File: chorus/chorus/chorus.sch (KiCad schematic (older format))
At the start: 17 parts, among them J1 IN, J3 Jack-DC, J4 OUT, SW1 SW_3PDT_x3, U2 TL074, U5 LM7805, U6 TL072, U8 TLE2426xLP

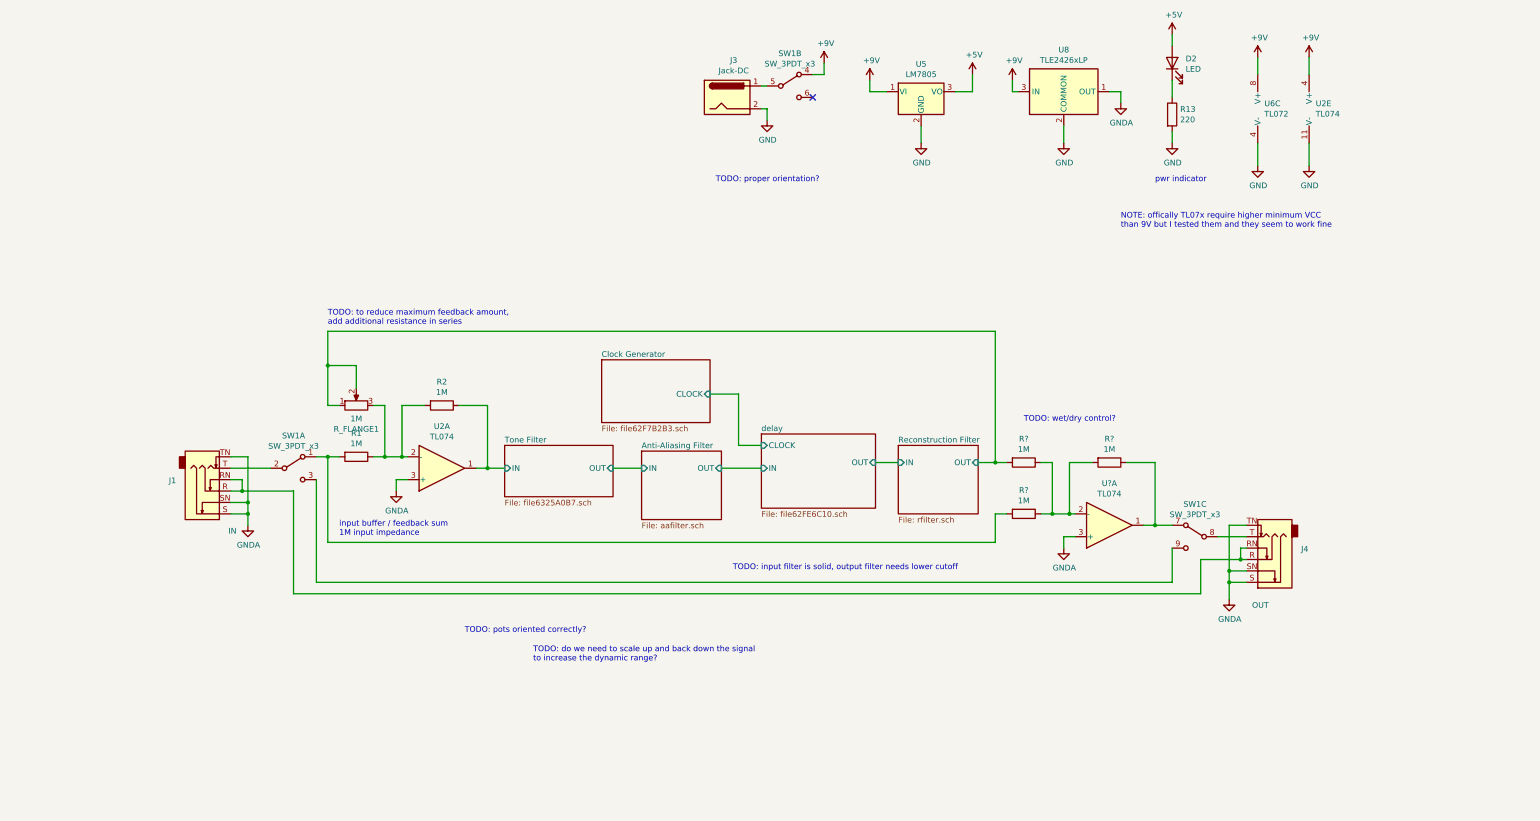
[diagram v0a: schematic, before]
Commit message: add wet/dry mix and recalculate filters
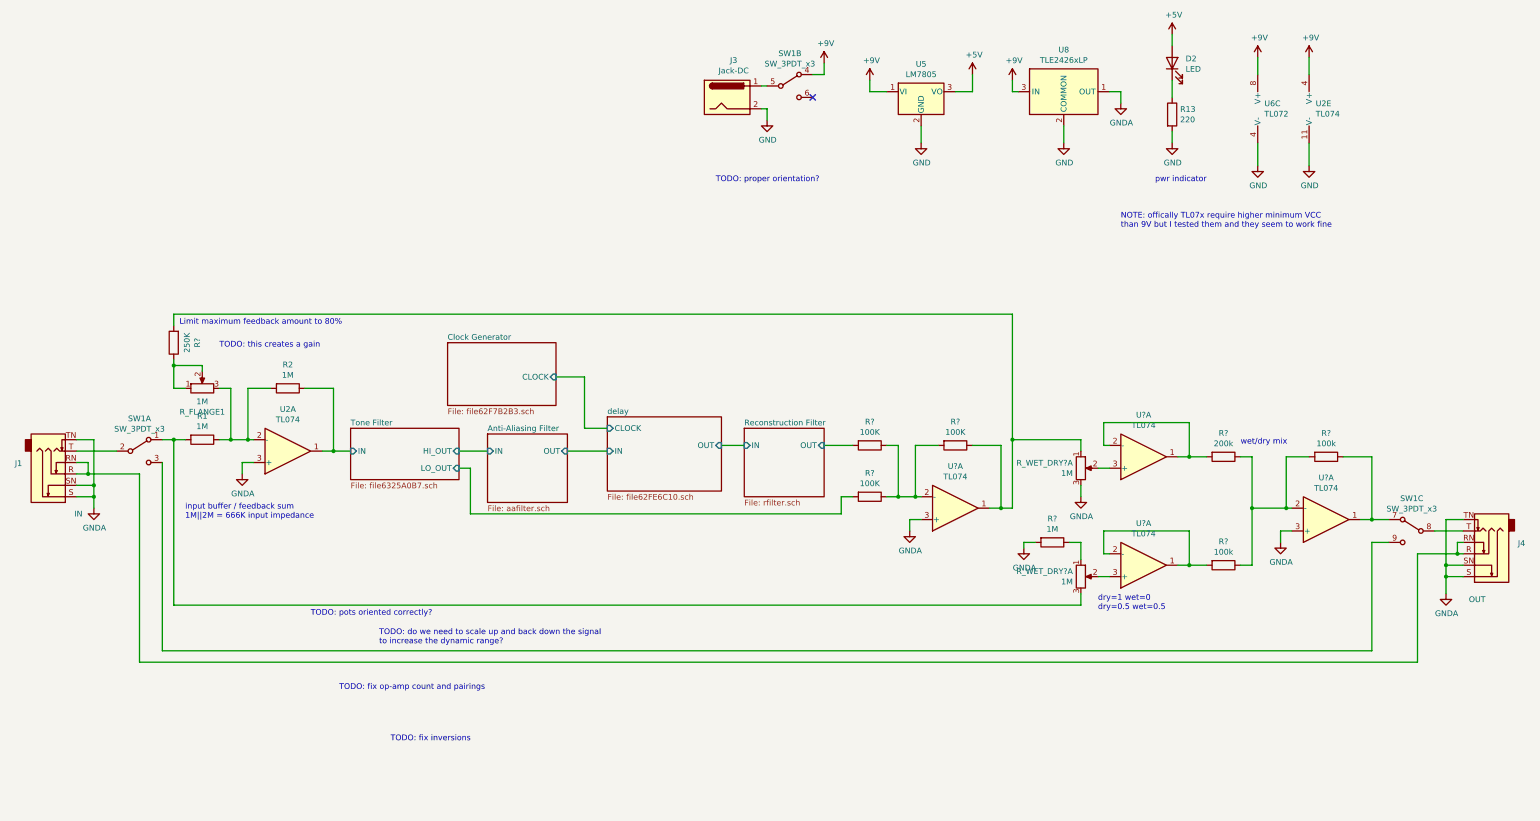
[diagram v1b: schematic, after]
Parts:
- removed R?: 1M, Resistor_THT:R_Axial_DIN0204_L3.6mm_D1.6mm_P2.54mm_Vertical, symbol Device:R
- added R?: 100K, Resistor_THT:R_Axial_DIN0204_L3.6mm_D1.6mm_P2.54mm_Vertical, symbol Device:R
- added R? (x2): 100k, Resistor_THT:R_Axial_DIN0204_L3.6mm_D1.6mm_P2.54mm_Vertical, symbol Device:R
- added R?: 1M, Resistor_THT:R_Axial_DIN0204_L3.6mm_D1.6mm_P2.54mm_Vertical, symbol Device:R
- added R?: 200k, Resistor_THT:R_Axial_DIN0204_L3.6mm_D1.6mm_P2.54mm_Vertical, symbol Device:R
- added R?: 250K, Resistor_THT:R_Axial_DIN0204_L3.6mm_D1.6mm_P2.54mm_Vertical, symbol Device:R
- added R_WET_DRY? (x2): 1M, symbol Device:R_POT_Dual_Separate
- added U? (x3): TL074, Package_DIP:DIP-14_W7.62mm, symbol Amplifier_Operational:TL074
- R? (x2): value 1M -> 100K
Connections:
- net GNDA: now also R?.2, R_WET_DRY?.3, U?.3 (+)
- net Reconstruction Filter/OUT: no longer R_FLANGE1.1, R_FLANGE1.2
- net at R1.2, SW1.1 (A): now also R_WET_DRY?.3
- net at R?.1, U?.1: now also R?.2, R_WET_DRY?.1; no longer SW1.7 (A)
- net at R?.1, R?.2, U?.2 (-): now also R?.1
- new net: R?.1, R_FLANGE1.1, R_FLANGE1.2
- new net: R?.1, SW1.7 (A), U?.1
- new net: R?.1, R?.1, R?.2, U?.2 (-)
- new net: R?.1, R_WET_DRY?.1
- new net: R?.2, U?.1, U?.2 (-) (x2)
- new net: R_WET_DRY?.2, U?.3 (+) (x2)
- new net Tone Filter/LO_OUT: R?.2
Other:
- note added: "Limit maximum feedback amount to 80%"
- note added: "TODO: fix inversions"
- note added: "TODO: fix op-amp count and pairings"
- note added: "TODO: this creates a gain"
- note added: "dry=1 wet=0\ndry=0.5 wet=0.5"
- note added: "input buffer / feedback sum\n1M||2M = 666K input impedance"
- note added: "wet/dry mix"
- note removed: "TODO: input filter is solid, output filter needs lower cutoff"
- note removed: "TODO: to reduce maximum feedback amount,\nadd additional resistance in series"
- note removed: "TODO: wet/dry control?"
- note removed: "input buffer / feedback sum\n1M input impedance"
- moved on the sheet: J1, J4, R1, R2, R?, R_FLANGE1, SW1A, SW1C, U2A, U?A

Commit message: update filters
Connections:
- net at R?.1, R_WET_DRY?.1, U?.1: no longer R?.2
- net at R?.2, U?.1, U?.2 (-): now also R?.2
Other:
- note added: "TODO: hard-code to 50/50 saves 2 op amps and a dual pot"
- note added: "TODO: probably too complex, but if tone filter became\nBP with only LP side tunable, and allowed high freqs\ncut by filters around the effect, would have a more consistent\ntone"
- note added: "filter+delay stage are all non-inverting,\nso low + high are in phase\n\ninput sum is inverting, then tone recombination is\ninverting, so wet + dry are in phase\n\nhowever end-to-end signal is inverted (by final sum/output buffer)"
- note added: "wet/dry mix\nmin: dry=1 wet=0\nmax: dry=0.5 wet=0.5"
- note removed: "TODO: fix inversions"
- note removed: "TODO: this creates a gain"
- note removed: "dry=1 wet=0\ndry=0.5 wet=0.5"
- note removed: "wet/dry mix"
- moved on the sheet: R?, U?A
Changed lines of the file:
@@
 L Amplifier_Operational:TL074 U?
 U 1 1 6282D08A
-P 7650 5050
-F 0 "U?" H 7650 4683 50  0000 C CNN
-F 1 "TL074" H 7650 4774 50  0000 C CNN
-F 2 "Package_DIP:DIP-14_W7.62mm" H 7600 5150 50  0001 C CNN
-F 3 "http://www.ti.com/lit/ds/symlink/tl071.pdf" H 7700 5250 50  0001 C CNN
-	1    7650 5050
-	1    0    0    1
-$EndComp
-Wire Wire Line
-	7250 5250 7250 5150
-Wire Wire Line
-	7250 5150 7350 5150
-Wire Wire Line
-	7350 4950 7300 4950
-Wire Wire Line
-	7300 4500 7300 4950
-Connection ~ 7300 4950
-Wire Wire Line
-	7300 4950 7150 4950
+P 7650 5200
+F 0 "U?" H 7650 4833 50  0000 C CNN
+F 1 "TL074" H 7650 4924 50  0000 C CNN
+F 2 "Package_DIP:DIP-14_W7.62mm" H 7600 5300 50  0001 C CNN
+F 3 "http://www.ti.com/lit/ds/symlink/tl071.pdf" H 7700 5400 50  0001 C CNN
+	1    7650 5200
+	1    0    0    1
+$EndComp
+Wire Wire Line
+	7250 5400 7250 5300
+Wire Wire Line
+	7250 5300 7350 5300
+Wire Wire Line
+	7350 5100 7300 5100
+Connection ~ 7300 5100
+Wire Wire Line
+	7300 5100 7150 5100
 $Comp
 L Device:R R?
 U 1 1 6282D0A4
-P 7650 4500
-F 0 "R?" V 7443 4500 50  0000 C CNN
-F 1 "100K" V 7534 4500 50  0000 C CNN
-F 2 "Resistor_THT:R_Axial_DIN0204_L3.6mm_D1.6mm_P2.54mm_Vertical" V 7580 4500 50  0001 C CNN
-F 3 "~" H 7650 4500 50  0001 C CNN
-	1    7650 4500
-	0    1    1    0
-$EndComp
-Wire Wire Line
-	7500 4500 7300 4500
-Wire Wire Line
-	7800 4500 8050 4500
-Wire Wire Line
-	8050 5050 7950 5050
+P 7650 4750
+F 0 "R?" V 7443 4750 50  0000 C CNN
+F 1 "100K" V 7534 4750 50  0000 C CNN
+F 2 "Resistor_THT:R_Axial_DIN0204_L3.6mm_D1.6mm_P2.54mm_Vertical" V 7580 4750 50  0001 C CNN
+F 3 "~" H 7650 4750 50  0001 C CNN
+	1    7650 4750
+	0    1    1    0
+$EndComp
+Wire Wire Line
+	8050 5200 7950 5200
 Wire Wire Line
 	7050 4500 7150 4500
@@
 L power:GNDA #PWR?
 U 1 1 6282D0C0
-P 7250 5250
-F 0 "#PWR?" H 7250 5000 50  0001 C CNN
-F 1 "GNDA" H 7255 5077 50  0000 C CNN
-F 2 "" H 7250 5250 50  0001 C CNN
-F 3 "" H 7250 5250 50  0001 C CNN
-	1    7250 5250
+P 7250 5400
+F 0 "#PWR?" H 7250 5150 50  0001 C CNN
+F 1 "GNDA" H 7255 5227 50  0000 C CNN
+F 2 "" H 7250 5400 50  0001 C CNN
+F 3 "" H 7250 5400 50  0001 C CNN
+	1    7250 5400
 	1    0    0    -1
 $EndComp
@@
 $EndComp
 Wire Wire Line
-	8050 5050 8050 4500
-Connection ~ 8050 5050
+	8050 5200 8050 4750
+Connection ~ 8050 5200
 Connection ~ 800  4450
 Wire Wire Line
@@
 L Device:R R?
 U 1 1 62A6A9A3
-P 6900 4950
-F 0 "R?" V 6693 4950 50  0000 C CNN
-F 1 "100K" V 6784 4950 50  0000 C CNN
-F 2 "Resistor_THT:R_Axial_DIN0204_L3.6mm_D1.6mm_P2.54mm_Vertical" V 6830 4950 50  0001 C CNN
-F 3 "~" H 6900 4950 50  0001 C CNN
-	1    6900 4950
+P 6900 5100
+F 0 "R?" V 6693 5100 50  0000 C CNN
+F 1 "100K" V 6784 5100 50  0000 C CNN
+F 2 "Resistor_THT:R_Axial_DIN0204_L3.6mm_D1.6mm_P2.54mm_Vertical" V 6830 5100 50  0001 C CNN
+F 3 "~" H 6900 5100 50  0001 C CNN
+	1    6900 5100
 	0    1    1    0
 $EndComp
@@
 Connection ~ 11300 5150
 Wire Wire Line
-	7050 4950 7150 4950
-Connection ~ 7150 4950
-Wire Wire Line
-	7150 4500 7150 4950
-Wire Wire Line
-	6750 4950 6650 4950
-Wire Wire Line
-	6650 4950 6650 5100
-Wire Wire Line
-	3400 5100 6650 5100
+	7050 5100 7150 5100
+Connection ~ 7150 5100
 Wire Wire Line
 	6500 4500 6750 4500
-Wire Wire Line
-	8150 5050 8150 4450
-Wire Wire Line
-	8150 5050 8050 5050
-Text Notes 8900 5950 0    50   ~ 0
-dry=1 wet=0\ndry=0.5 wet=0.5
-Text Notes 10150 4500 0    50   ~ 0
-wet/dry mix
+Text Notes 8800 5100 0    50   ~ 0
+wet/dry mix\nmin: dry=1 wet=0\nmax: dry=0.5 wet=0.5
 Text Notes 2250 6650 0    50   ~ 0
 TODO: fix op-amp count and pairings
-Text Notes 2700 7100 0    50   ~ 0
-TODO: fix inversions
 $Comp
 L Amplifier_Operational:TL074 U?
@@
 L power:GNDA #PWR?
 U 1 1 62B4A803
-P 8750 4950
-F 0 "#PWR?" H 8750 4700 50  0001 C CNN
-F 1 "GNDA" H 8755 4777 50  0000 C CNN
-F 2 "" H 8750 4950 50  0001 C CNN
-F 3 "" H 8750 4950 50  0001 C CNN
-	1    8750 4950
-	1    0    0    -1
+P 8750 4450
+F 0 "#PWR?" H 8750 4200 50  0001 C CNN
+F 1 "GNDA" H 8755 4277 50  0000 C CNN
+F 2 "" H 8750 4450 50  0001 C CNN
+F 3 "" H 8750 4450 50  0001 C CNN
+	1    8750 4450
+	-1   0    0    1
 $EndComp
 Wire Wire Line
@@
 Connection ~ 9700 4600
 Wire Wire Line
-	9700 4600 9850 4600
+	9700 4600 9800 4600
 $Comp
 L Device:R_POT_Dual_Separate R_WET_DRY?
@@
 F 3 "~" H 8750 4700 50  0001 C CNN
 	1    8750 4700
-	1    0    0    -1
+	1    0    0    1
 $EndComp
 Wire Wire Line
@@
 L power:GNDA #PWR?
 U 1 1 62BC944D
-P 8250 5400
-F 0 "#PWR?" H 8250 5150 50  0001 C CNN
-F 1 "GNDA" H 8255 5227 50  0000 C CNN
-F 2 "" H 8250 5400 50  0001 C CNN
-F 3 "" H 8250 5400 50  0001 C CNN
-	1    8250 5400
+P 8000 5400
+F 0 "#PWR?" H 8000 5150 50  0001 C CNN
+F 1 "GNDA" H 8005 5227 50  0000 C CNN
+F 2 "" H 8000 5400 50  0001 C CNN
+F 3 "" H 8000 5400 50  0001 C CNN
+	1    8000 5400
 	1    0    0    -1
 $EndComp
 Wire Wire Line
-	8250 5400 8250 5350
-Wire Wire Line
-	8250 5350 8350 5350
-Wire Wire Line
 	8650 5350 8750 5350
 Wire Wire Line
 	8750 5350 8750 5500
-Wire Wire Line
-	8750 4950 8750 4850
 Wire Wire Line
 	8750 5800 8750 5900
@@
 Wire Wire Line
 	10250 5050 10250 4600
-Wire Wire Line
-	8750 4550 8750 4450
-Wire Wire Line
-	8750 4450 8150 4450
-Connection ~ 8150 4450
-Wire Wire Line
-	8150 3350 8150 4450
-Wire Wire Line
-	800  3350 8150 3350
 $Comp
 L Device:R R?
@@
 Wire Wire Line
 	800  3800 800  4000
-Text Notes 1200 3650 0    50   ~ 0
-TODO: this creates a gain
 Wire Wire Line
 	700  6300 11300 6300
@@
 Wire Wire Line
 	11700 5450 11700 6400
+Wire Wire Line
+	7150 4500 7150 5100
+Wire Wire Line
+	7500 4750 7300 4750
+Wire Wire Line
+	7300 4750 7300 5100
+Wire Wire Line
+	7800 4750 8050 4750
+Wire Wire Line
+	3400 5100 6750 5100
+Wire Wire Line
+	8750 4550 8750 4450
+Wire Wire Line
+	8750 4850 8750 5200
+Wire Wire Line
+	8000 5400 8000 5350
+Wire Wire Line
+	8000 5350 8350 5350
+Text Notes 9000 6000 0    50   ~ 0
+TODO: hard-code to 50/50 saves 2 op amps and a dual pot
+Text Notes 2400 5650 0    50   ~ 0
+TODO: probably too complex, but if tone filter became\nBP with only LP side tunable, and allowed high freqs\ncut by filters around the effect, would have a more consistent\ntone
+Wire Wire Line
+	8050 5200 8750 5200
+Wire Wire Line
+	9800 4600 9800 3350
+Wire Wire Line
+	800  3350 9800 3350
+Connection ~ 9800 4600
+Wire Wire Line
+	9800 4600 9850 4600
+Text Notes 4900 4000 0    50   ~ 0
+filter+delay stage are all non-inverting,\nso low + high are in phase\n\ninput sum is inverting, then tone recombination is\ninverting, so wet + dry are in phase\n\nhowever end-to-end signal is inverted (by final sum/output buffer)
 $EndSCHEMATC

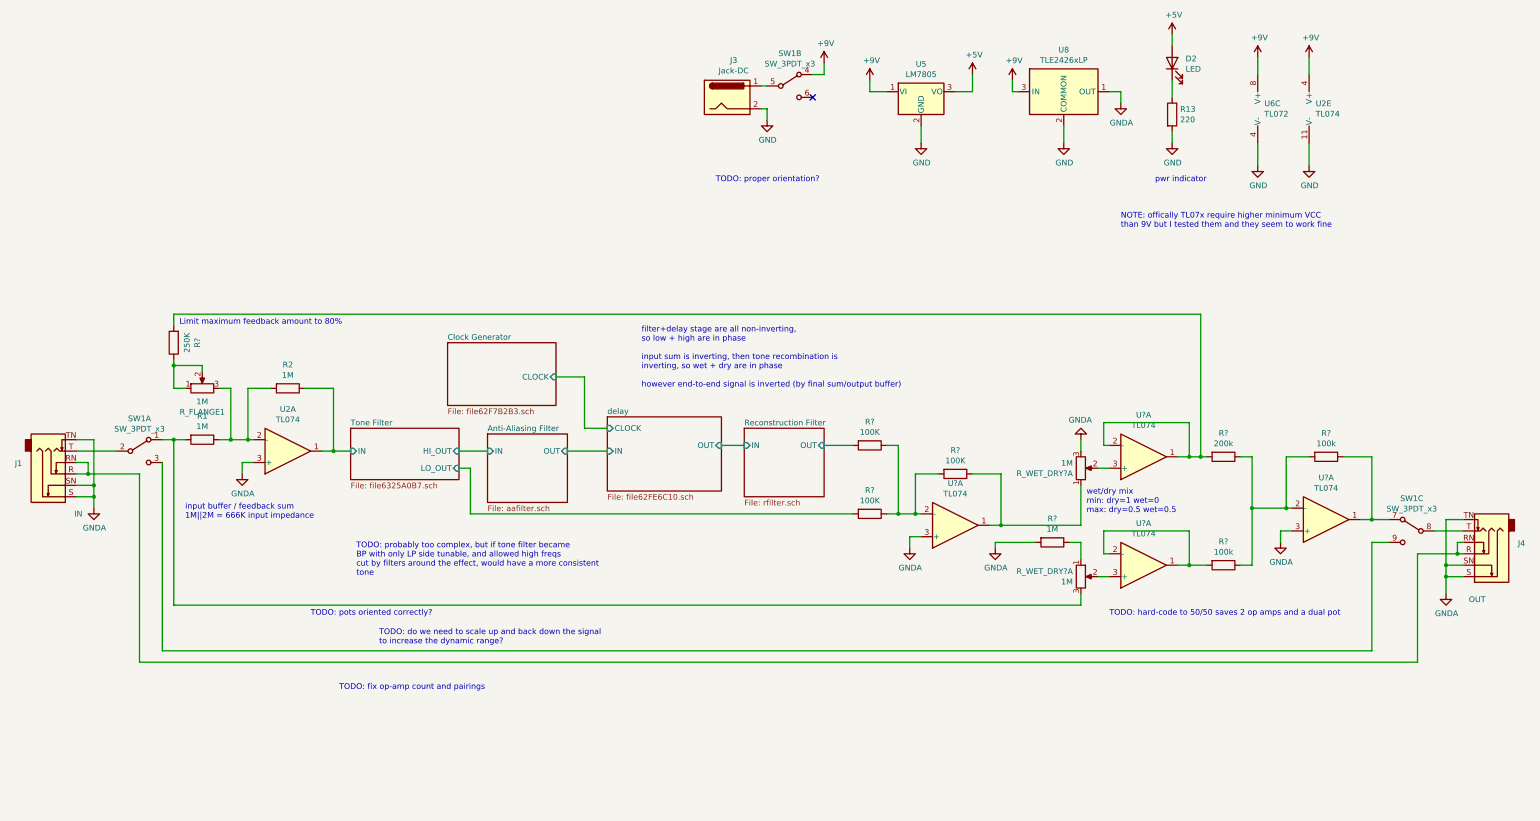
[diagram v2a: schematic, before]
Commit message: remove dry/wet, add higher dry frequencies
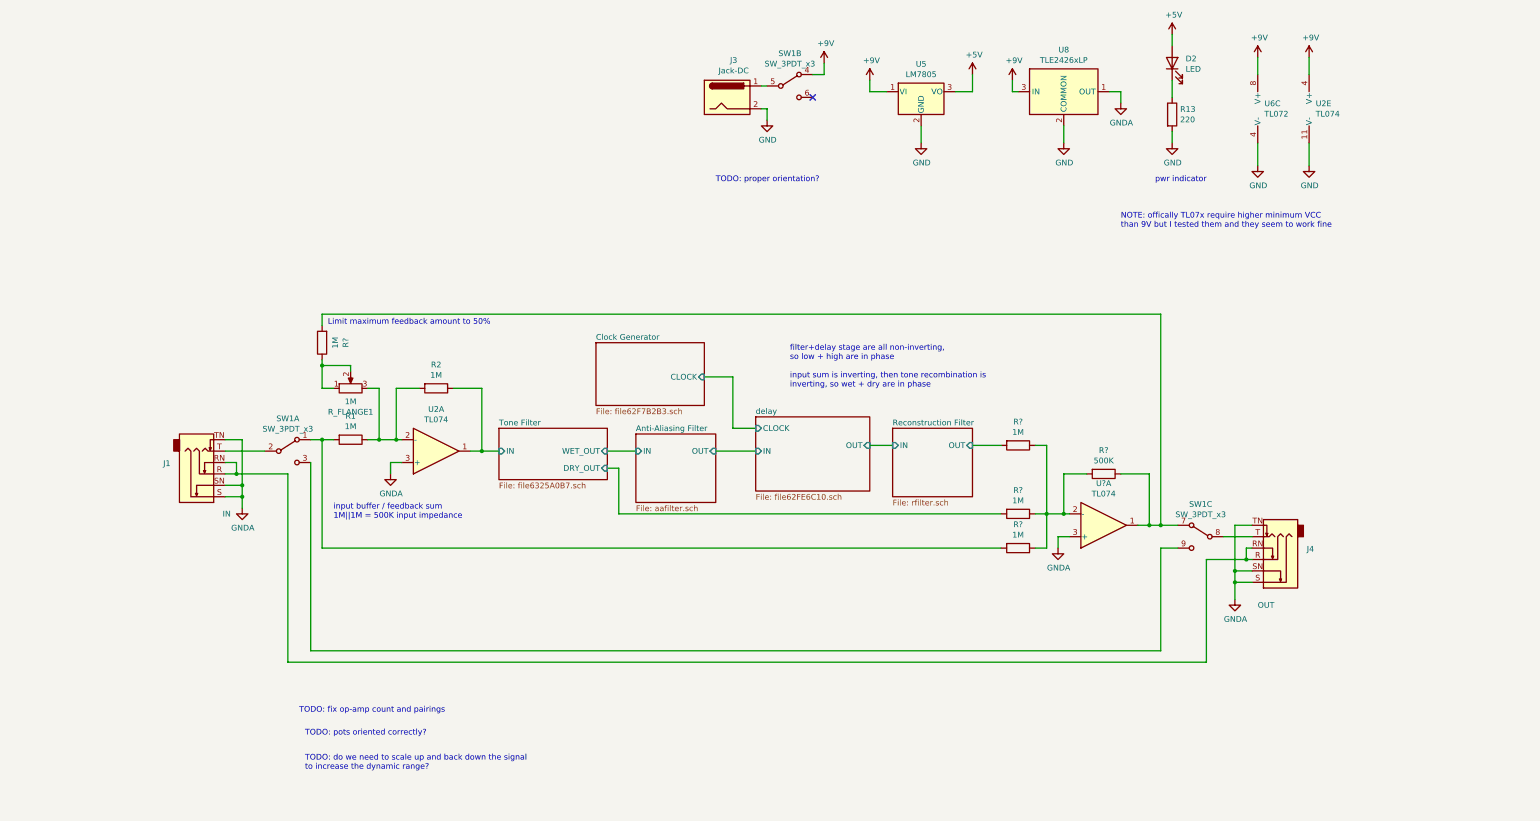
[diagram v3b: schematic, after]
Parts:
- removed R? (x2): 100k, Resistor_THT:R_Axial_DIN0204_L3.6mm_D1.6mm_P2.54mm_Vertical, symbol Device:R
- removed R?: 200k, Resistor_THT:R_Axial_DIN0204_L3.6mm_D1.6mm_P2.54mm_Vertical, symbol Device:R
- removed R_WET_DRY? (x2): 1M, symbol Device:R_POT_Dual_Separate
- removed U? (x3): TL074, Package_DIP:DIP-14_W7.62mm, symbol Amplifier_Operational:TL074
- R?: value 100K -> 500K
- R? (x2): value 100K -> 1M
- R?: value 250K -> 1M
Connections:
- net GNDA: no longer R?.2
- net at R1.2, SW1.1 (A): now also R?.2
- net at R?.1, U?.1: now also R?.2, SW1.7 (A)
- net at R?.1, R?.1, R?.2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: now also R?.1
- net Tone Filter/LO_OUT renamed Tone Filter/DRY_OUT
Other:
- note added: "Limit maximum feedback amount to 50%"
- note added: "filter+delay stage are all non-inverting,\nso low + high are in phase\n\ninput sum is inverting, then tone recombination is\ninverting, so wet + dry are in phase"
- note added: "input buffer / feedback sum\n1M||1M = 500K input impedance"
- note removed: "Limit maximum feedback amount to 80%"
- note removed: "TODO: hard-code to 50/50 saves 2 op amps and a dual pot"
- note removed: "TODO: probably too complex, but if tone filter became\nBP with only LP side tunable, and allowed high freqs\ncut by filters around the effect, would have a more consistent\ntone"
- note removed: "filter+delay stage are all non-inverting,\nso low + high are in phase\n\ninput sum is inverting, then tone recombination is\ninverting, so wet + dry are in phase\n\nhowever end-to-end signal is inverted (by final sum/output buffer)"
- note removed: "input buffer / feedback sum\n1M||2M = 666K input impedance"
- note removed: "wet/dry mix\nmin: dry=1 wet=0\nmax: dry=0.5 wet=0.5"
- moved on the sheet: J1, J4, R1, R2, R?, R_FLANGE1, SW1A, SW1C, U2A, U?A

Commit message: improve BP calculations imperically
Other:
- note added: "sum half dry signal plus half wet signal"
- note added: "todo: tone filter has a smaller filter\nwhich with the aggressive filters\ncreates a notch at ~2-3KHz (depending on tone pos)\nis this a problem? Making a 8th order filter to fix it doesn’t\nseem worthwhile…"
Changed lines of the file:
@@
 Wire Wire Line
 	8050 5400 2100 5400
+Text Notes 4400 6900 0    50   ~ 0
+todo: tone filter has a smaller filter\nwhich with the aggressive filters\ncreates a notch at ~2-3KHz (depending on tone pos)\nis this a problem? Making a 8th order filter to fix it doesn’t\nseem worthwhile…
+Text Notes 7700 5700 0    50   ~ 0
+sum half dry signal plus half wet signal
 $EndSCHEMATC
